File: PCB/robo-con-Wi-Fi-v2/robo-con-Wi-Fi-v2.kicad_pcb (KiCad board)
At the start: 4 copper layers, 86 x 67 mm, 108 parts, among them J1 Conn_01x04, J2 SMA-J, J3 Conn_01x05, J4 Conn_01x01, J5 Conn_01x02, J6 Conn_01x01, J7 Conn_01x06, J8 Conn_01x01, J9 Conn_01x01, SW1 SW_Push, SW2 SW_Slide, U1 STM32H723VGTx, U10 MCP73831-2-OT, U11 LM66100DCK, U15 LM66100DCK, U18 USB_Type-C, U2 LBEE5HY2FY, U3 FT234XD, U4 MCP1727-1802xMF, U5 RKJXV122400R, U6 LD39200PU33R, U7 RKJXV122400R, U8 TMHU28, U9 TMHU28, Y2 XRCGB25M000FFS1AR0

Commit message: PCB
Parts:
- added D2: ESD, Diode_SMD:D_0603_1608Metric_Pad1.05x0.95mm_HandSolder, F.Cu at (181.1, 49.2)
- added D4: ESD, Diode_SMD:D_0603_1608Metric_Pad1.05x0.95mm_HandSolder, F.Cu at (185.7, 49.2)
- added G***: LOGO, LOGO, F.Cu at (142.8, 52.8)
- C82: value 1u -> 10u; footprint Capacitor_SMD:C_0402_1005Metric_Pad0.74x0.62mm_HandSolder -> Capacitor_SMD:C_0603_1608Metric_Pad1.08x0.95mm_HandSolder
- moved R25 102.3 mm to (192.1, 67.1)
- moved C18 99.3 mm to (187.3, 55.8)
- moved L1 96.3 mm to (178.6, 53.2), turned to 90 degrees
- moved C81 95.2 mm to (196.2, 58.8), turned to -90 degrees
- moved R5 93.9 mm to (184.8, 51.2), turned to -90 degrees
- moved SW2 93.9 mm to (201.4, 62.5), turned to 90 degrees
- moved C14 92.7 mm to (198.0, 65.4)
- moved C17 92.6 mm to (180.6, 54.1), turned to 90 degrees
- moved C15 92.5 mm to (198.0, 61.1)
- moved C79 92.1 mm to (180.0, 56.1), turned to 180 degrees
- moved C13 91.7 mm to (197.2, 54.7), turned to 90 degrees
- moved R3 90.9 mm to (181.9, 51.2), turned to -90 degrees
- moved R43 89.7 mm to (176.7, 47.5), turned to -90 degrees
- moved C82 89.3 mm to (190.5, 57.4), turned to 90 degrees
- moved C12 89.2 mm to (194.7, 54.1)
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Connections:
- C12 pad 2: +3.3V -> GND
- C13 pad 2: +3.3V -> GND
- C14 pad 2: +3.3V -> GND
- C15 pad 2: +3.3V -> GND
- C16 pad 2: +3.3V -> GND
- C17 pad 2: +3.3V -> GND
- C18 pad 2: +3.3V -> GND
- C19 pad 2: +3.3V -> GND
- C28 pad 2: +3.3V -> GND
- C30 pad 2: +3.3V -> GND
- C31 pad 2: +3.3V -> GND
- C33 pad 2: +3.3V -> GND
- C34 pad 2: +3.3V -> GND
- C35 pad 2: +3.3V -> GND
- C50 pad 2: +3.3V -> GND
- C57 pad 2: +3.3V -> GND
- C58 pad 2: +3.3V -> GND
- C61 pad 2: +3.3V -> GND
- C62 pad 2: +3.3V -> GND
- C63 pad 2: +3.3V -> GND
- C64 pad 2: +3.3V -> GND
- C65 pad 2: +3.3V -> GND
- C66 pad 2: +3.3V -> GND
- C67 pad 2: +3.3V -> GND
- C68 pad 2: +3.3V -> GND
- C69 pad 2: +3.3V -> GND
- C70 pad 2: +3.3V -> GND
- C71 pad 2: +3.3V -> GND
- C72 pad 2: +3.3V -> GND
- C73 pad 2: +3.3V -> GND
- C74 pad 2: +3.3V -> GND
- C75 pad 2: +3.3V -> GND
- C76 pad 2: +3.3V -> GND
- C77 pad 2: +3.3V -> GND
- C78 pad 2: +3.3V -> GND
- C79 pad 2: +3.3V -> GND
- C80 pad 2: +3.3V -> GND
- C81 pad 2: +3.3V -> GND
- C82 pad 2: +3.3V -> GND
- C83 pad 2: +3.3V -> GND
- D11 pad 1: +3.3V -> GND
- J1 pad 1: +3.3V -> GND
- J2 pad 2: +3.3V -> GND
- J3 pad 5: +3.3V -> GND
- J5 pad 2: +3.3V -> GND
- J6 pad 1: +3.3V -> GND
- J7 pad 6: +3.3V -> GND
- J9 pad 1: +3.3V -> GND
- R1 pad 5: +3.3V -> GND
- R1 pad 6: +3.3V -> GND
- R1 pad 7: +3.3V -> GND
- R1 pad 8: +3.3V -> GND
- R23 pad 2: +3.3V -> GND
- R24 pad 2: +3.3V -> GND
- R26 pad 2: +3.3V -> GND
- R28 pad 2: +3.3V -> GND
- R29 pad 2: +3.3V -> GND
- R30 pad 2: +3.3V -> GND
- R31 pad 5: +3.3V -> GND
- R31 pad 6: +3.3V -> GND
- R31 pad 7: +3.3V -> GND
- R31 pad 8: +3.3V -> GND
- R39 pad 2: +3.3V -> GND
- R40 pad 2: +3.3V -> GND
- R43 pad 2: +3.3V -> GND
- R7 pad 2: +3.3V -> GND
- SW1 pad 1: +3.3V -> GND
- SW2 pad 1: +3.3V -> GND
- U1 pad 10: +3.3V -> GND
- U1 pad 19: +3.3V -> GND
- U1 pad 26: +3.3V -> GND
- U1 pad 49: +3.3V -> GND
- U1 pad 55: unconnected-(U1-PD8-Pad55) -> Serial_RXD
- U1 pad 56: unconnected-(U1-PD9-Pad56) -> Serial_TXD
- U1 pad 58: unconnected-(U1-PD11-Pad58) -> Serial_RTS
- U1 pad 59: unconnected-(U1-PD12-Pad59) -> Serial_CTS
- U1 pad 68: unconnected-(U1-PA9-Pad68) -> BT_UART_RXD
- U1 pad 69: unconnected-(U1-PA10-Pad69) -> BT_UART_TXD
- U1 pad 70: unconnected-(U1-PA11-Pad70) -> BT_UART_RTS
- U1 pad 71: unconnected-(U1-PA12-Pad71) -> BT_UART_CTS
- U1 pad 74: +3.3V -> GND
- U1 pad 99: +3.3V -> GND
- U10 pad 2: +3.3V -> GND
- U11 pad 2: +3.3V -> GND
- U11 pad 3: +3.3V -> GND
- U11 pad 5: +3.3V -> GND
- U15 pad 2: +3.3V -> GND
- U15 pad 3: +3.3V -> GND
- U15 pad 5: +3.3V -> GND
- U18 pad A1: +3.3V -> GND
- U18 pad B1: +3.3V -> GND
- U18 pad S1: +3.3V -> GND
- U2 pad 10: +3.3V -> GND
- U2 pad 12: +3.3V -> GND
- U2 pad 13: +3.3V -> GND
- U2 pad 19: +3.3V -> GND
- U2 pad 21: +3.3V -> GND
- U2 pad 24: +3.3V -> GND
- U2 pad 26: +3.3V -> GND
- U2 pad 27: +3.3V -> GND
- U2 pad 29: +3.3V -> GND
- U2 pad 39: +3.3V -> GND
- U2 pad 44: +3.3V -> GND
- U2 pad 49: +3.3V -> GND
- U2 pad 51: +3.3V -> GND
- U2 pad 52: +3.3V -> GND
- U2 pad 53: +3.3V -> GND
- U2 pad 55: +3.3V -> GND
- U2 pad 56: +3.3V -> GND
- U2 pad 58: +3.3V -> GND
- U2 pad 59: +3.3V -> GND
- U2 pad 60: +3.3V -> GND
- U2 pad 61: +3.3V -> GND
- U2 pad 66: +3.3V -> GND
- U2 pad 67: +3.3V -> GND
- U2 pad 68: +3.3V -> GND
- U2 pad 69: +3.3V -> GND
- U2 pad 70: +3.3V -> GND
- U2 pad 71: +3.3V -> GND
- U2 pad 72: +3.3V -> GND
- U3 pad 10: Serial_TX -> Serial_RXD
- U3 pad 11: Serial_RTS -> Serial_CTS
- U3 pad 13: +3.3V -> GND
- U3 pad 5: +3.3V -> GND
- U3 pad 7: Serial_RX -> Serial_TXD
- U3 pad 8: Serial_CTS -> Serial_RTS
- U4 pad 4: +3.3V -> GND
- U4 pad 9: +3.3V -> GND
- U5 pad 1: +3.3V -> GND
- U5 pad 4: +3.3V -> GND
- U6 pad 3: +3.3V -> GND
- U6 pad 7: +3.3V -> GND
- U7 pad 1: +3.3V -> GND
- U7 pad 4: +3.3V -> GND
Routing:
- net +5V: track 0.00 -> 56.7 mm, vias 0 -> 1
- net +1V8: track 0.00 -> 50.0 mm, vias 0 -> 2
- net BT_UART_CTS: track 0.00 -> 38.0 mm, vias 0 -> 2
- net BT_UART_RTS: track 0.00 -> 37.4 mm, vias 0 -> 2
- net BT_UART_RXD: track 0.00 -> 36.5 mm, vias 0 -> 2
- net +3.3V: track 0.00 -> 35.6 mm
- net BT_UART_TXD: track 0.00 -> 34.6 mm, vias 0 -> 2
- net Serial_RXD: track 0.00 -> 33.4 mm, vias 0 -> 2
- net Serial_CTS: track 0.00 -> 32.7 mm, vias 0 -> 2
- net Serial_TXD: track 0.00 -> 30.2 mm, vias 0 -> 2
- net Serial_RTS: track 0.00 -> 30.2 mm, vias 0 -> 2
- net SDMMC1_D2: track 0.00 -> 28.3 mm
- net SDMMC1_CMD: track 0.00 -> 28.3 mm
- net SDMMC1_D0: track 0.00 -> 25.3 mm, vias 0 -> 2
- net SDMMC1_D1: track 0.00 -> 25.3 mm, vias 0 -> 2
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- added copper zone on B.Cu, net GND
- added copper zone on F.Cu, net GND
- added copper zone on In1.Cu, net GND
- added copper zone on In2.Cu, net GND
- removed copper zone on B.Cu, net +3.3V
- removed copper zone on F.Cu, net +3.3V
- removed copper zone on In1.Cu, net +3.3V
- removed copper zone on In2.Cu, net +3.3V

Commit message: v2 配線
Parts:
- removed R1, R31: WA04X102, My_Library:WA04X102
- removed R28, R29: 10k, Resistor_SMD:R_0603_1608Metric_Pad0.98x0.95mm_HandSolder
- removed R30, R47, R7: 1k, Resistor_SMD:R_0402_1005Metric_Pad0.72x0.64mm_HandSolder
- added D15: W, Diode_SMD:D_0603_1608Metric_Pad1.05x0.95mm_HandSolder, F.Cu at (200.7, 49.4)
- added D17: O, Diode_SMD:D_0603_1608Metric_Pad1.05x0.95mm_HandSolder, F.Cu at (152.4, 55.3)
- added D18: R, Diode_SMD:D_0603_1608Metric_Pad1.05x0.95mm_HandSolder, F.Cu at (152.4, 61.4)
- added R12: 10k, Resistor_SMD:R_0402_1005Metric_Pad0.72x0.64mm_HandSolder, F.Cu at (164.8, 87.4)
- added R13: 10k, Resistor_SMD:R_0402_1005Metric_Pad0.72x0.64mm_HandSolder, F.Cu at (164.8, 86.2)
- added R14: 10k, Resistor_SMD:R_0402_1005Metric_Pad0.72x0.64mm_HandSolder, F.Cu at (170.2, 87.4)
- added R15: 10k, Resistor_SMD:R_0402_1005Metric_Pad0.72x0.64mm_HandSolder, F.Cu at (170.2, 86.2)
- added R22: 1k, Resistor_SMD:R_0402_1005Metric_Pad0.72x0.64mm_HandSolder, F.Cu at (200.7, 52.6)
- added R34: 1k, Resistor_SMD:R_0402_1005Metric_Pad0.72x0.64mm_HandSolder, F.Cu at (156.2, 55.3)
- added R36: 1k, Resistor_SMD:R_0402_1005Metric_Pad0.72x0.64mm_HandSolder, F.Cu at (156.2, 61.4)
- F1: value box -> FHC16322ADTP
- SW2: value SW_Slide -> SS-12D00G3
- moved R21 109.1 mm to (198.7, 52.6), turned to 90 degrees
- moved D11 93.9 mm to (198.7, 49.4), turned to -90 degrees
- moved R4 68.6 mm to (156.2, 44.4)
- moved R2 68.6 mm to (156.2, 42.2)
- moved R6 68.3 mm to (156.2, 46.6)
- moved R11 67.8 mm to (156.2, 48.7)
- moved R35 66.9 mm to (156.2, 59.2)
- moved R33 65.2 mm to (156.2, 53.1)
- moved R32 65.1 mm to (156.2, 50.9)
- moved D1 51.4 mm to (152.4, 42.2), turned to 180 degrees
- moved D3 51.3 mm to (152.4, 44.4), turned to 180 degrees
- moved D5 51.2 mm to (152.4, 46.6), turned to 180 degrees
- moved D10 51.1 mm to (152.4, 48.7), turned to 180 degrees
- moved D16 49.2 mm to (152.4, 59.2), turned to 180 degrees
- moved R44 48.5 mm to (175.4, 66.6), turned to -90 degrees
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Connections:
- D1 pad 1: LED0 -> Net-(D1-K)
- D1 pad 2: Net-(D1-A) -> +3.3V
- D10 pad 1: LED3 -> Net-(D10-K)
- D10 pad 2: Net-(D10-A) -> +3.3V
- D13 pad 1: LED4 -> Net-(D13-K)
- D13 pad 2: Net-(D13-A) -> +3.3V
- D14 pad 1: LEDWL -> Net-(D14-K)
- D14 pad 2: Net-(D14-A) -> +3.3V
- D16 pad 1: LEDLiPo -> Net-(D16-K)
- D16 pad 2: Net-(D16-A) -> +3.3V
- D3 pad 1: LED1 -> Net-(D3-K)
- D3 pad 2: Net-(D3-A) -> +3.3V
- D5 pad 1: LED2 -> Net-(D5-K)
- D5 pad 2: Net-(D5-A) -> +3.3V
- J3 pad 2: R5_BUTTON -> L5_BUTTON
- J3 pad 3: R6_BUTTON -> L6_BUTTON
- J3 pad 4: R7_BUTTON -> L7_BUTTON
- J7 pad 2: L1_BUTTON -> R1_BUTTON
- J7 pad 3: L2_BUTTON -> R2_BUTTON
- J7 pad 4: L3_BUTTON -> R3_BUTTON
- J7 pad 5: L4_BUTTON -> R4_BUTTON
- R11 pad 1: +3.3V -> Net-(D10-K)
- R11 pad 2: Net-(D10-A) -> LED3
- R2 pad 1: +3.3V -> Net-(D1-K)
- R2 pad 2: Net-(D1-A) -> LED0
- R32 pad 1: +3.3V -> Net-(D13-K)
- R32 pad 2: Net-(D13-A) -> LED4
- R33 pad 1: +3.3V -> Net-(D14-K)
- R33 pad 2: Net-(D14-A) -> LEDWL
- R35 pad 1: +3.3V -> Net-(D16-K)
- R35 pad 2: Net-(D16-A) -> LEDLiPo_GOOD
- R4 pad 1: +3.3V -> Net-(D3-K)
- R4 pad 2: Net-(D3-A) -> LED1
- R44 pad 5: SDMMC1_CMD -> SDMMC1_D2
- R44 pad 6: SDMMC1_CLK -> SDMMC1_D3
- R44 pad 7: SDMMC1_D3 -> SDMMC1_CLK
- R44 pad 8: unconnected-(R44-Pad8) -> SDMMC1_CMD
- R6 pad 1: +3.3V -> Net-(D5-K)
- R6 pad 2: Net-(D5-A) -> LED2
- U1 pad 1: unconnected-(U1-PE2-Pad1) -> L0_LEVER
- U1 pad 2: unconnected-(U1-PE3-Pad2) -> L2_LEVER
- U1 pad 28: unconnected-(U1-PA4-Pad28) -> LY_STICK
- U1 pad 29: unconnected-(U1-PA5-Pad29) -> LX_STICK
- U1 pad 3: unconnected-(U1-PE4-Pad3) -> L1_LEVER
- U1 pad 30: unconnected-(U1-PA6-Pad30) -> LP_STICK
- U1 pad 33: unconnected-(U1-PC5-Pad33) -> LiPo_OBSERVE
- U1 pad 34: unconnected-(U1-PB0-Pad34) -> RX_STICK
- U1 pad 35: unconnected-(U1-PB1-Pad35) -> RY_STICK
- U1 pad 4: unconnected-(U1-PE5-Pad4) -> L3_LEVER
- U1 pad 47: unconnected-(U1-PB11-Pad47) -> RP_STICK
- U1 pad 5: unconnected-(U1-PE6-Pad5) -> L4_LEVER
- U1 pad 51: unconnected-(U1-PB12-Pad51) -> R1_BUTTON
- U1 pad 52: unconnected-(U1-PB13-Pad52) -> R2_BUTTON
- U1 pad 53: unconnected-(U1-PB14-Pad53) -> R3_BUTTON
- U1 pad 54: unconnected-(U1-PB15-Pad54) -> R4_BUTTON
- U1 pad 57: unconnected-(U1-PD10-Pad57) -> R4_LEVER
- U1 pad 60: unconnected-(U1-PD13-Pad60) -> R3_LEVER
- U1 pad 61: unconnected-(U1-PD14-Pad61) -> R0_LEVER
- U1 pad 62: unconnected-(U1-PD15-Pad62) -> R2_LEVER
- U1 pad 63: unconnected-(U1-PC6-Pad63) -> R1_LEVER
- U1 pad 7: unconnected-(U1-PC13-Pad7) -> L5_BUTTON
- U1 pad 8: unconnected-(U1-PC14-Pad8) -> L6_BUTTON
- U1 pad 86: unconnected-(U1-PD5-Pad86) -> WL_ON
- U1 pad 87: unconnected-(U1-PD6-Pad87) -> BT_ON
- U1 pad 89: unconnected-(U1-PB3(JTDO-Pad89) -> LED0
- U1 pad 9: unconnected-(U1-PC15-Pad9) -> L7_BUTTON
- U1 pad 90: unconnected-(U1-PB4(NJTRST)-Pad90) -> LED1
- U1 pad 91: unconnected-(U1-PB5-Pad91) -> LED2
- U1 pad 92: unconnected-(U1-PB6-Pad92) -> LED3
- U1 pad 93: unconnected-(U1-PB7-Pad93) -> LED4
- U1 pad 95: unconnected-(U1-PB8-Pad95) -> LEDWL
- U1 pad 96: unconnected-(U1-PB9-Pad96) -> LEDUSB
- U1 pad 97: unconnected-(U1-PE0-Pad97) -> LEDLiPo_GOOD
- U1 pad 98: unconnected-(U1-PE1-Pad98) -> LEDLiPo_BAD
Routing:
- net +1V8: track 50.0 -> 407.8 mm, vias 2 -> 8
- net +3.3V: track 35.6 -> 131.0 mm, vias 0 -> 2
- net NRST: track 0.00 -> 93.7 mm, vias 0 -> 2
- net R4_LEVER: track 0.00 -> 65.9 mm, vias 0 -> 2
- net R2_LEVER: track 0.00 -> 63.7 mm, vias 0 -> 2
- net R0_LEVER: track 0.00 -> 62.1 mm, vias 0 -> 2
- net R3_LEVER: track 0.00 -> 62.1 mm, vias 0 -> 2
- net R1_LEVER: track 0.00 -> 61.7 mm, vias 0 -> 2
- net L4_LEVER: track 0.00 -> 56.4 mm, vias 0 -> 2
- net L3_LEVER: track 0.00 -> 55.5 mm, vias 0 -> 2
- net L1_LEVER: track 0.00 -> 54.0 mm, vias 0 -> 2
- net RY_STICK: track 0.00 -> 53.4 mm, vias 0 -> 1
- net L2_LEVER: track 0.00 -> 52.8 mm, vias 0 -> 2
- net L0_LEVER: track 0.00 -> 51.6 mm, vias 0 -> 2
- net SWCLK: track 2.91 -> 54.2 mm
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
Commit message: 一応　配線とシルク完了
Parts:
- moved D11 3.12 mm to (199.6, 46.5)
- moved D15 3.12 mm to (201.7, 46.5)
- moved G*** 3.07 mm to (140.8, 51.3)
- moved G*** 2.49 mm to (134.4, 46.7)
- moved R21 1.21 mm to (199.6, 51.8)
- moved R22 1.21 mm to (201.7, 51.8)
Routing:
- net Net-(D15-A): track 1.67 -> 3.85 mm
- net Net-(D11-A): track 1.67 -> 3.85 mm
- net GND: track 15.3 -> 16.2 mm
- net +3.3V: track 131.0 -> 130.7 mm, vias 2 -> 4
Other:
- board text added: "+3.3V"
- board text added: "+VBUS"
- board text added: "BAD"
- board text added: "GOOD"
- board text added: "LED0"
- board text added: "LED1"
- board text added: "LED2"
- board text added: "LED3"
- board text added: "LED4"
- board text added: "LEDUSB"
- board text added: "LEDWL"
- board text added: "LiPo"
- board text added: "NRST"
- board text added: "R2"
- board text added: "SWCLK"
- board text added: "SWDIO"
- board text added: "指定なしはC1"
- board text removed: "+5V"
- board text removed: "C1"
- board text removed: "C6.5"

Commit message: PCB
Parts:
- removed J3: Conn_01x05, Connector_JST:JST_ZH_B5B-ZR_1x05_P1.50mm_Vertical
- removed R12, R13, R14, R15: 10k, Resistor_SMD:R_0402_1005Metric_Pad0.72x0.64mm_HandSolder
- added J10: Conn_01x06, Connector_JST:JST_ZH_B6B-ZR_1x06_P1.50mm_Vertical, F.Cu at (134.7, 59.1)
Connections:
- U1 pad 15: unconnected-(U1-PC0-Pad15) -> L8_BUTTON
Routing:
- net L8_BUTTON: track 0.00 -> 33.5 mm, vias 0 -> 1
- net RX_STICK: track 47.9 -> 41.2 mm
- net RY_STICK: track 53.4 -> 47.7 mm
- net LY_STICK: track 21.5 -> 16.1 mm
- net LX_STICK: track 35.3 -> 31.3 mm

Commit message: update
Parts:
- removed C57: 1u, Capacitor_SMD:C_0402_1005Metric_Pad0.74x0.62mm_HandSolder
- removed C58, C67: 0.1u, Capacitor_SMD:C_0402_1005Metric_Pad0.74x0.62mm_HandSolder
- removed SW2: SS-12D00G3, 0Ikedalibrary:swich_SS-12D00G3
- removed U1: STM32H723VGTx, Package_QFP:LQFP-100_14x14mm_P0.5mm
- removed U9: TMHU28, My_Library:TMHU28
- added SW3: SW_Push, My_Library:SKHHLPA010, F.Cu at (133.5, 29.6)
- added SW4: SW_Push, My_Library:SKHHLPA010, F.Cu at (206.5, 29.6)
- added SW5: SW_Push_SPDT, My_Library:4MS1R202M6QES, F.Cu at (188.8, 44.0)
- added SW6: SW_Push_SPDT, My_Library:8MS8P1B05VS2QES-C13, F.Cu at (153.0, 56.0)
- added SW7: SW_Push_SPDT, My_Library:8MS8P1B05VS2QES-C13, F.Cu at (187.0, 56.0)
- J8, J9: moved to F.Cu
- SW1: moved to B.Cu
- U8: value TMHU28 -> STM32H7A3RGTx; footprint My_Library:TMHU28 -> Package_QFP:LQFP-64_10x10mm_P0.5mm
- moved J4 134.3 mm to (85.0, 98.7), turned to 0 degrees
- moved J8 128.7 mm to (91.1, 98.7), turned to 0 degrees
- moved J6 126.3 mm to (88.1, 98.7), turned to 0 degrees
- moved J9 120.9 mm to (94.2, 98.7), turned to 0 degrees
- moved D11 116.9 mm to (90.1, 87.4), turned to 0 degrees
- moved D15 113.8 mm to (94.5, 84.8), turned to 0 degrees
- moved R22 113.4 mm to (98.3, 98.4), turned to 0 degrees
- moved R21 110.7 mm to (98.3, 96.4), turned to 0 degrees
- moved U6 110.5 mm to (92.0, 103.4)
- moved D4 109.0 mm to (85.7, 92.6), turned to 0 degrees
- moved U15 107.9 mm to (98.7, 104.8), turned to 0 degrees
- moved U11 106.5 mm to (98.7, 101.3)
- moved D2 102.7 mm to (85.7, 87.4)
- moved D12 101.5 mm to (90.1, 90.0), turned to 0 degrees
- moved C15 95.0 mm to (103.6, 71.9)
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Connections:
- J10 pad 1: +1V8 -> GND
- J10 pad 2: L5_BUTTON -> L8_BUTTON
- J10 pad 3: L6_BUTTON -> L7_BUTTON
- J10 pad 4: L7_BUTTON -> L6_BUTTON
- J10 pad 5: L8_BUTTON -> L5_BUTTON
- J10 pad 6: GND -> +1V8
- U8 pad 1: L1_LEVER -> +1V8
- U8 pad 2: L2_LEVER -> unconnected-(U8-PC13-Pad2)
- U8 pad 3: L3_LEVER -> unconnected-(U8-PC14-Pad3)
- U8 pad 4: L4_LEVER -> unconnected-(U8-PC15-Pad4)
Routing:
- net +1V8: track 407.8 -> 4.34 mm, vias 8 -> 0
- net +3.3V: track 130.7 -> 7.20 mm, vias 4 -> 0
- net NRST: track 93.7 -> 0.00 mm, vias 2 -> 0
- net R4_LEVER: track 65.9 -> 0.00 mm, vias 2 -> 0
- net R2_LEVER: track 63.7 -> 0.00 mm, vias 2 -> 0
- net R0_LEVER: track 62.1 -> 0.00 mm, vias 2 -> 0
- net R3_LEVER: track 62.1 -> 0.00 mm, vias 2 -> 0
- net R1_LEVER: track 61.7 -> 0.00 mm, vias 2 -> 0
- net +5V: track 58.3 -> 0.00 mm, vias 1 -> 0
- net L4_LEVER: track 56.4 -> 0.00 mm, vias 2 -> 0
- net L3_LEVER: track 55.5 -> 0.00 mm, vias 2 -> 0
- net SWDIO: track 54.4 -> 0.00 mm, vias 1 -> 0
- net SWCLK: track 54.2 -> 0.00 mm, vias 1 -> 0
- net L1_LEVER: track 54.0 -> 0.00 mm, vias 2 -> 0
- net L2_LEVER: track 52.8 -> 0.00 mm, vias 2 -> 0
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- removed copper zone on B.Cu, net GND
- removed copper zone on F.Cu, net GND
- removed copper zone on In1.Cu, net GND
- removed copper zone on In2.Cu, net GND
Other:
- board size 86 x 67 mm -> 86 x 62 mm
- board text removed: "+3.3V"
- board text removed: "+VBUS"
- board text removed: "BAD"
- board text removed: "GND"
- board text removed: "GOOD"
- board text removed: "LED0"
- board text removed: "LED1"
- board text removed: "LED2"
- board text removed: "LED3"
- board text removed: "LED4"
- board text removed: "LEDUSB"
- board text removed: "LEDWL"
- board text removed: "LiPo"
- board text removed: "NRST"
- board text removed: "SWCLK"
- board text removed: "SWDIO"
- board text removed: "robo-con-Wi-Fi-v2"

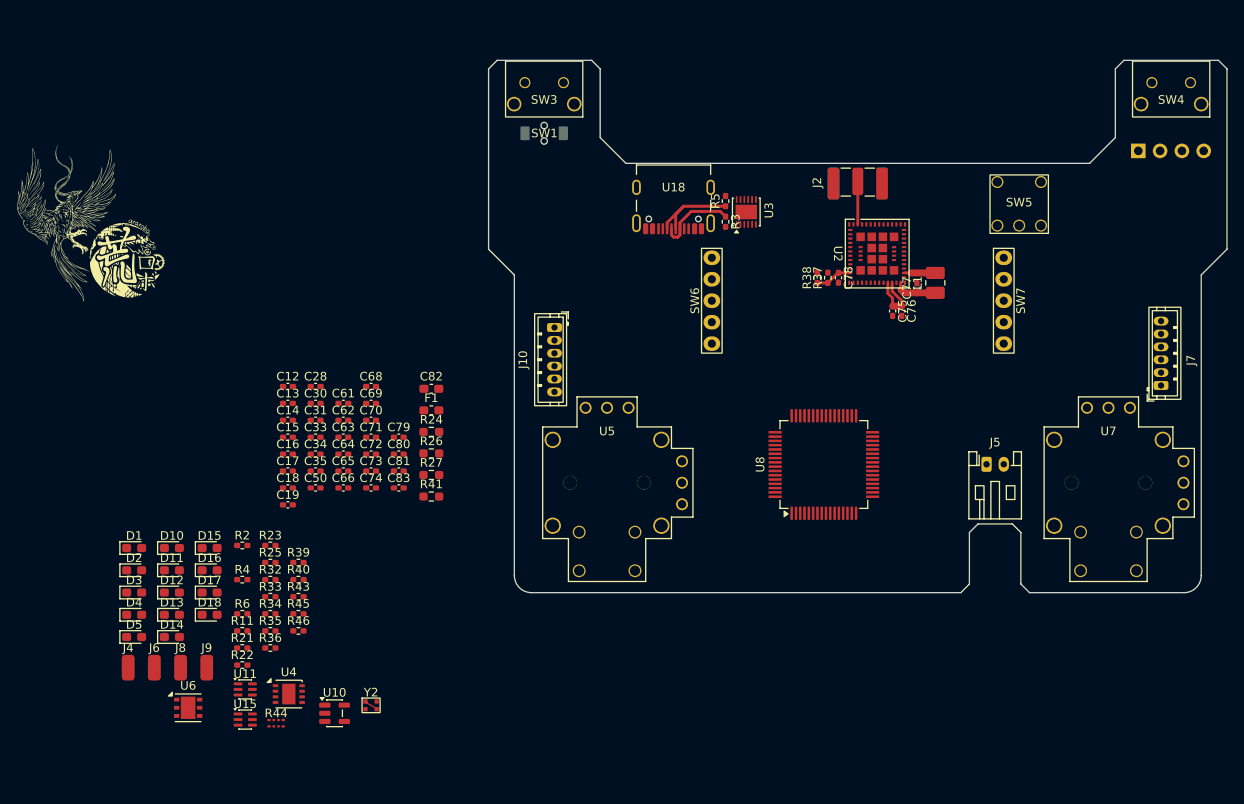
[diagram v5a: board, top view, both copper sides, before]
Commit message: move v2 program file & update PCB
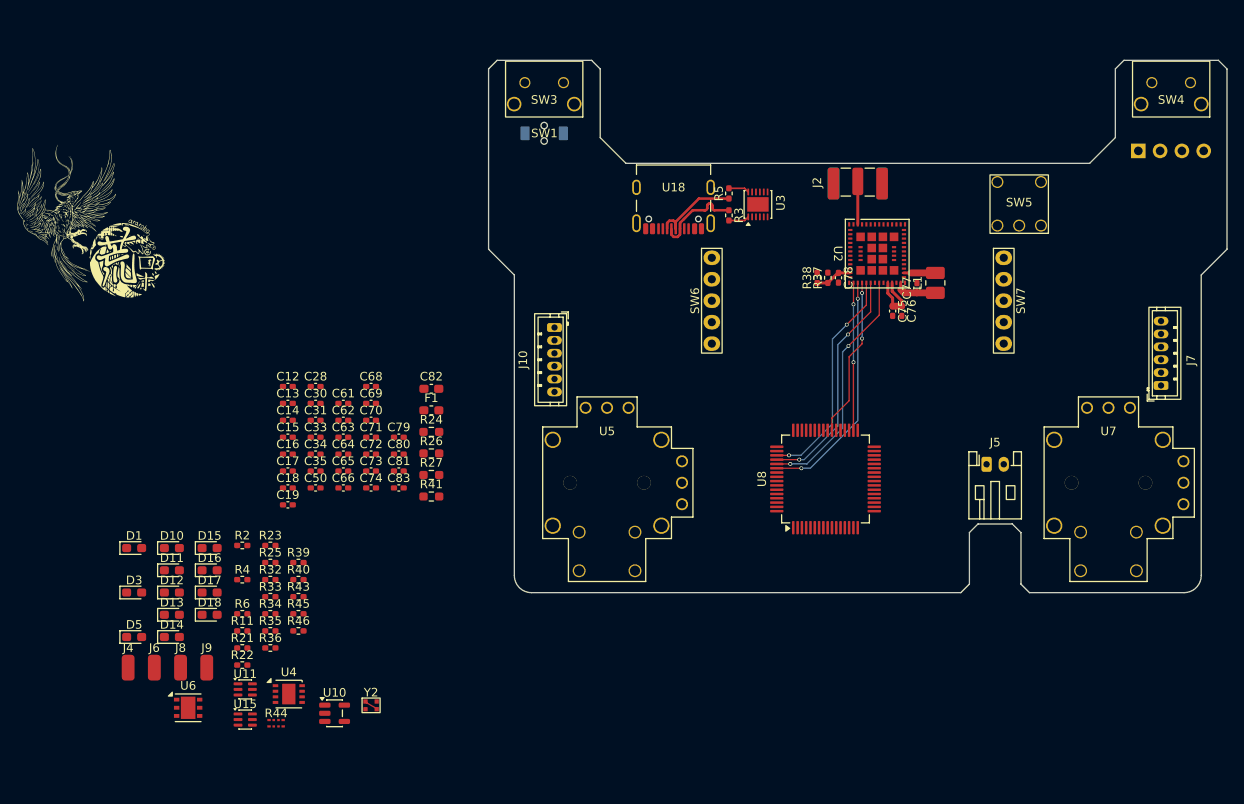
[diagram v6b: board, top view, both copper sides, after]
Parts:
- removed D2, D4: ESD, Diode_SMD:D_0603_1608Metric_Pad1.05x0.95mm_HandSolder
- J1: footprint Connector_PinSocket_2.54mm:PinSocket_1x04_P2.54mm_Horizontal -> Connector_PinSocket_2.54mm:PinSocket_1x04_P2.54mm_Vertical
- moved U8 1.70 mm to (166.2, 76.8)
- moved U3 1.62 mm to (158.4, 44.8)
- moved R5 0.98 mm to (155.0, 43.5)
- moved R3 0.84 mm to (155.0, 46.1)
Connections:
- U8 pad 14: unconnected-(U8-PA0-Pad14) -> BT_UART_RTS
- U8 pad 15: unconnected-(U8-PA1-Pad15) -> BT_UART_CTS
- U8 pad 16: unconnected-(U8-PA2-Pad16) -> BT_UART_RXD
- U8 pad 17: unconnected-(U8-PA3-Pad17) -> BT_UART_TXD
- U8 pad 41: unconnected-(U8-PA9-Pad41) -> Serial_RXD
- U8 pad 42: unconnected-(U8-PA10-Pad42) -> Serial_TXD
- U8 pad 43: unconnected-(U8-PA11-Pad43) -> Serial_RTS
- U8 pad 44: unconnected-(U8-PA12-Pad44) -> Serial_CTS
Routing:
- net SDMMC1_CLK: track 0.00 -> 28.1 mm, vias 0 -> 2
- net SDMMC1_CMD: track 0.00 -> 27.8 mm, vias 0 -> 2
- net SDMMC1_D3: track 0.00 -> 27.0 mm, vias 0 -> 2
- net SDMMC1_D2: track 0.00 -> 26.1 mm, vias 0 -> 2
- net SDMMC1_D1: track 0.00 -> 18.6 mm, vias 0 -> 2
- net SDMMC1_D0: track 0.00 -> 17.2 mm, vias 0 -> 2
- net USB_DP: track 0.00 -> 2.43 mm
- net USB_DN: track 0.00 -> 2.43 mm
- net Net-(R3-Pad1): track 9.45 -> 10.7 mm
- net Net-(R5-Pad1): track 11.3 -> 10.7 mm
